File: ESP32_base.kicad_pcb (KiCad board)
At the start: 2 copper layers, 112 x 54.9 mm, 32 parts, among them J1 Conn_01x16_Socket, J2 Conn_01x16_Socket, J3 Conn_01x04_Socket, J5 KH-IPEXA-SMAKWE-B080H, SW1 boot, SW2 reset, U1 ADT7310TRZ, U2 3.3V, U3 ESP32-C5-WROOM-1U-N8-R4

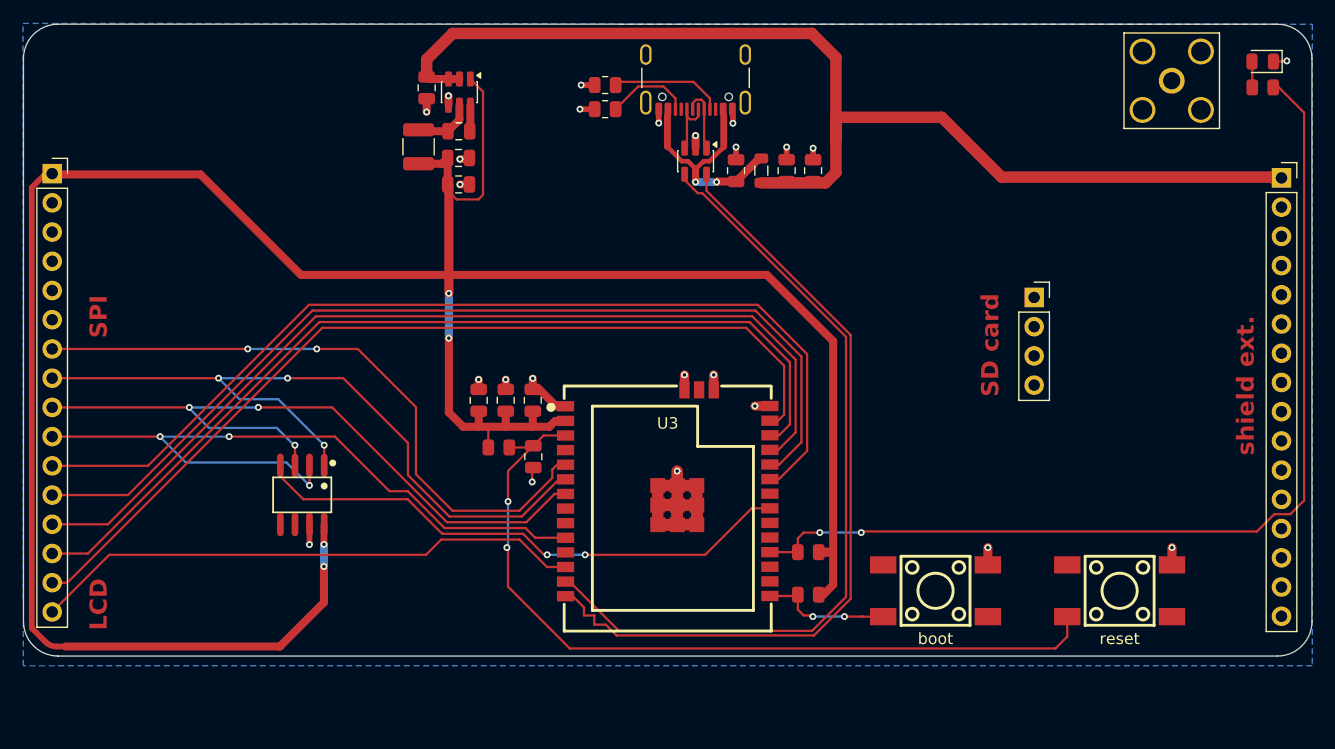
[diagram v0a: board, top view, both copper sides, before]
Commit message: increase signal clearance
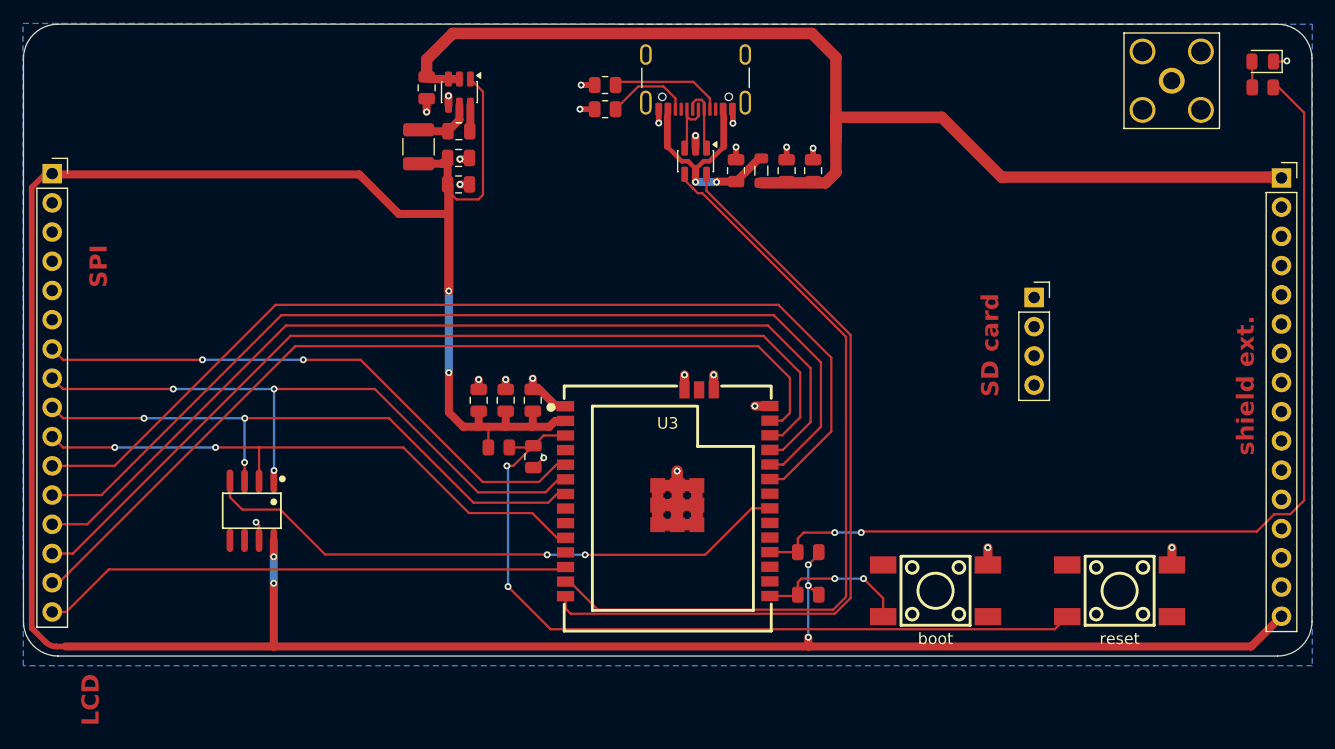
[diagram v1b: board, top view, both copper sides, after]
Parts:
- moved U1 4.59 mm to (103.4, 234.3)
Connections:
- J2 pad 16: unconnected-(J2-Pin_16-Pad16) -> +3.3V
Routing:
- net +3.3V: track 228.7 -> 262.8 mm, vias 4 -> 7
- net /SPI_MISO: track 64.9 -> 51.2 mm, vias 3 -> 2
- net /SPI_SCK: track 65.8 -> 56.6 mm
- net /SPI_MOSI: track 62.4 -> 53.8 mm
- net /JOYSTICK: track 55.9 -> 50.0 mm
- net /TEMP_CS: track 47.4 -> 52.1 mm
- net /TP_IRQ: track 85.5 -> 88.5 mm
- net Net-(U3-EN): track 71.6 -> 69.5 mm
- net /TP_CS: track 84.1 -> 86.1 mm
- net /LCD_DC: track 48.2 -> 46.2 mm
- net Net-(U3-IO28): track 11.5 -> 13.4 mm
- net /USB_D-: track 70.2 -> 68.6 mm
- net /USB_D+: track 70.2 -> 68.6 mm
- net /LCD_BL: track 79.5 -> 78.5 mm
- net /LCD_RST: track 82.5 -> 83.5 mm

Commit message: route EN across MCU
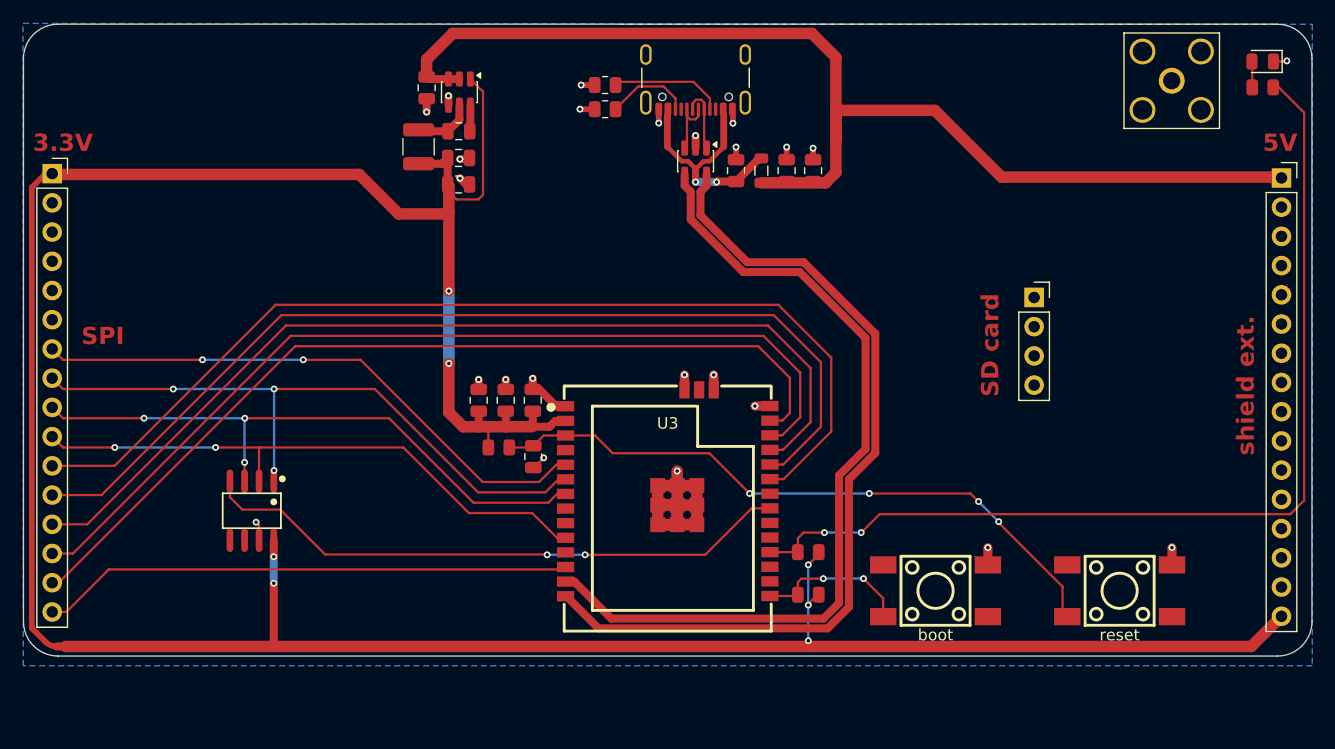
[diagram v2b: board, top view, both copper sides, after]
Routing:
- net Net-(U3-EN): track 69.5 -> 56.8 mm, vias 2 -> 4
- net /USB_D-: track 68.6 -> 74.5 mm
- net /USB_D+: track 68.6 -> 73.3 mm
- net +5V: track 101.9 -> 102.7 mm
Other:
- board text added: "3.3V"
- board text added: "5V"
- board text removed: "LCD"

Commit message: cleanup lower left corner
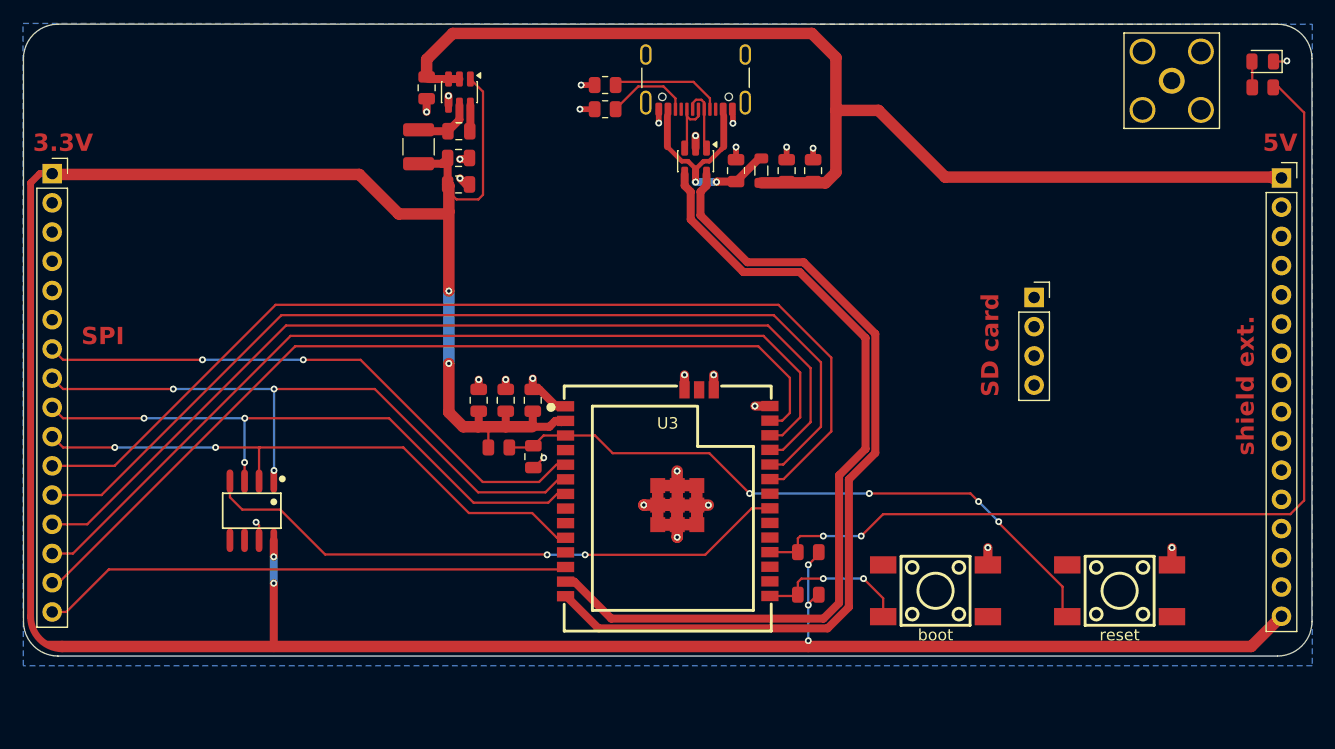
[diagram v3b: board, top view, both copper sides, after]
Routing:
- net +3.3V: track 262.4 -> 258.6 mm
- net GND: track 58.2 -> 61.5 mm, vias 24 -> 27
- net +5V: track 102.7 -> 100.1 mm

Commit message: wip
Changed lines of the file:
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@@
 			)
 		)
-		(property "Datasheet" "~"
+		(property "Datasheet" "https://www.lcsc.com/datasheet/C2905421.pdf"
 			(at 0 0 0)
 			(layer "F.Fab")
@@
 			)
 		)
-		(property "Description" "Generic connector, single row, 01x16, script generated"
+		(property "Description" "Female Header 16 Position 2.54mm Pitch Single Row Through Hole -40℃~+105℃"
 			(at 0 0 0)
 			(layer "F.Fab")
@@
 			)
 		)
+		(property "Part" "KH-2.54FH-1X16P-H8.5"
+			(at 0 0 0)
+			(unlocked yes)
+			(layer "F.Fab")
+			(hide yes)
+			(effects
+				(font
+					(size 1 1)
+					(thickness 0.15)
+				)
+			)
+		)
 		(property ki_fp_filters "Connector*:*_1x??_*")
 		(sheetname "/")
@@
 			)
 		)
-		(property "Datasheet" "~"
+		(property "Datasheet" "https://www.lcsc.com/datasheet/C2905421.pdf"
 			(at 0 0 0)
 			(layer "F.Fab")
@@
 			)
 		)
-		(property "Description" "Generic connector, single row, 01x16, script generated"
+		(property "Description" "Female Header 16 Position 2.54mm Pitch Single Row Through Hole -40℃~+105℃"
 			(at 0 0 0)
 			(layer "F.Fab")
@@
 			)
 		)
+		(property "Part" "KH-2.54FH-1X16P-H8.5"
+			(at 0 0 0)
+			(unlocked yes)
+			(layer "F.Fab")
+			(hide yes)
+			(effects
+				(font
+					(size 1 1)
+					(thickness 0.15)
+				)
+			)
+		)
 		(property ki_fp_filters "Connector*:*_1x??_*")
 		(sheetname "/")
@@
 	)
 	(segment
-		(start 122.3 234.5)
-		(end 127.8 234.5)
+		(start 104.1 228.8)
+		(end 116.6 228.8)
 		(width 0.2)
 		(layer "F.Cu")
@@
 	)
 	(segment
-		(start 104.1 228.8)
-		(end 116.6 228.8)
+		(start 122.3 234.5)
+		(end 127.96 234.5)
 		(width 0.2)
 		(layer "F.Cu")
@@
 	)
 	(segment
-		(start 127.8 234.5)
-		(end 129.95 236.65)
+		(start 91.52 228.8)
+		(end 87.0186 228.8)
 		(width 0.2)
 		(layer "F.Cu")
@@
 	)
 	(segment
-		(start 129.95 236.65)
-		(end 130.7 236.65)
+		(start 127.96 234.5)
+		(end 130.11 236.65)
 		(width 0.2)
 		(layer "F.Cu")
@@
 	)
 	(segment
-		(start 116.6 228.8)
-		(end 122.3 234.5)
+		(start 130.11 236.65)
+		(end 130.7 236.65)
 		(width 0.2)
 		(layer "F.Cu")
@@
 	)
 	(segment
-		(start 91.52 228.8)
-		(end 87.0186 228.8)
+		(start 116.6 228.8)
+		(end 122.3 234.5)
 		(width 0.2)
 		(layer "F.Cu")

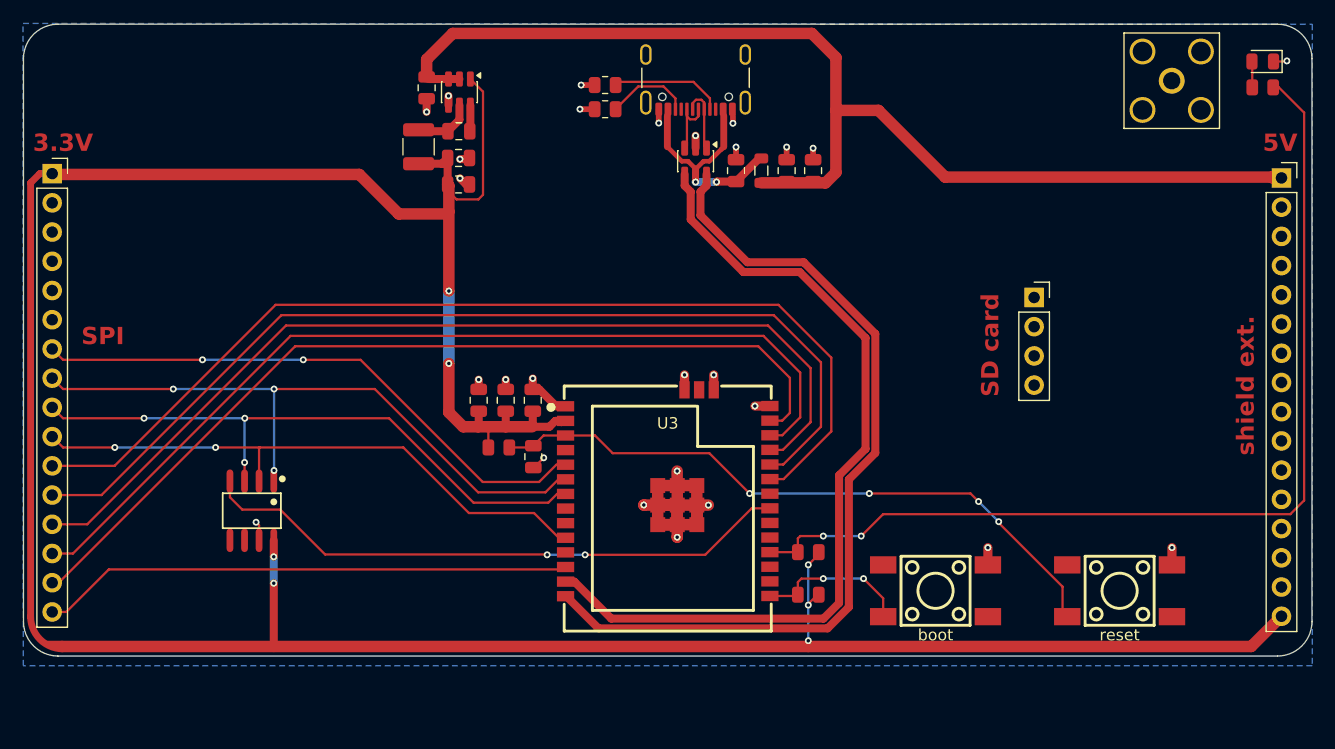
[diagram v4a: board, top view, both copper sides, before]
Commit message: 1206 -> 0805 and no ERC errors
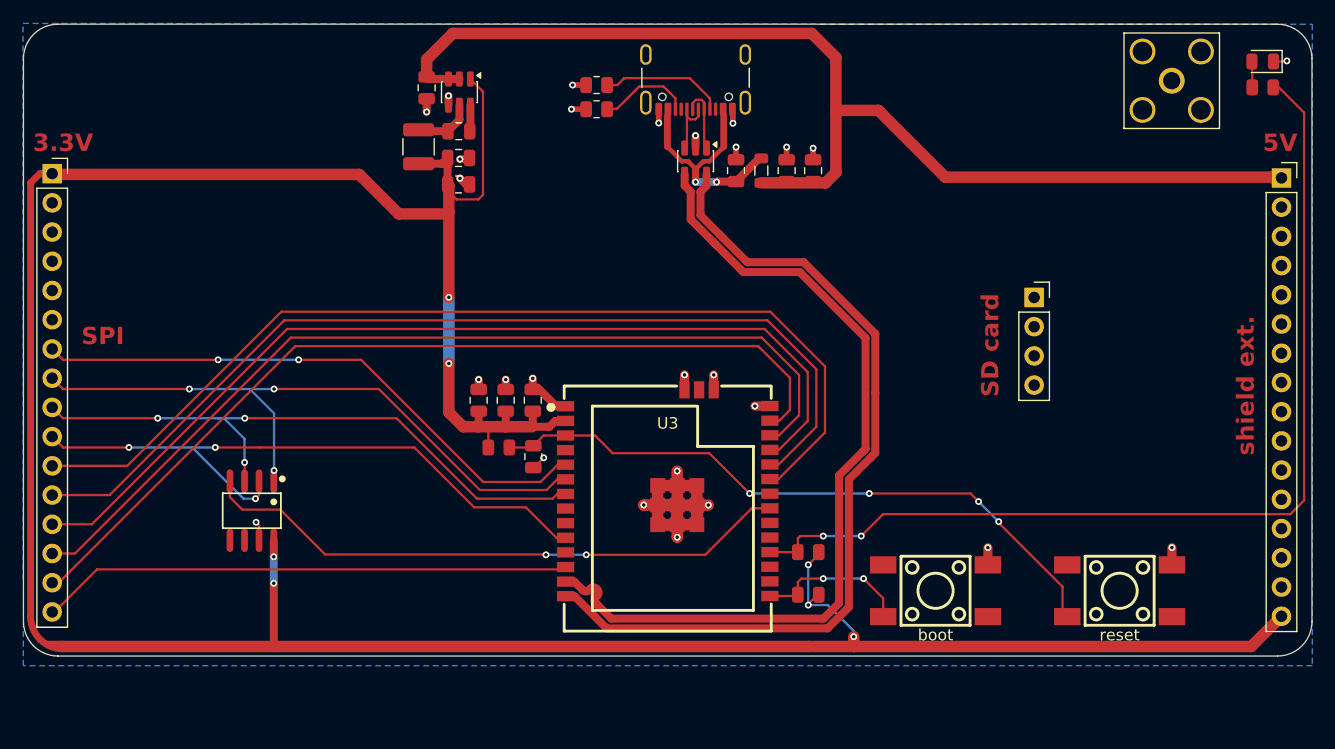
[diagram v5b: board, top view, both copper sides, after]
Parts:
- moved R1 0.74 mm to (133.4, 197.3)
- moved R2 0.74 mm to (133.4, 199.4)
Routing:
- net /SPI_MISO: track 51.2 -> 57.3 mm, vias 2 -> 3
- net +3.3V: track 258.6 -> 260.8 mm
- net /TP_IRQ: track 88.5 -> 86.5 mm
- net /TP_CS: track 86.1 -> 84.6 mm
- net /USB_D+: track 73.3 -> 74.5 mm
- net /LCD_RST: track 83.5 -> 82.5 mm
- net /SPI_MOSI: track 53.8 -> 54.8 mm
- net Net-(USBC1-CC1): track 9.69 -> 10.7 mm
- net /SPI_SCK: track 56.6 -> 57.3 mm
- net /LCD_CS: track 81.0 -> 80.5 mm

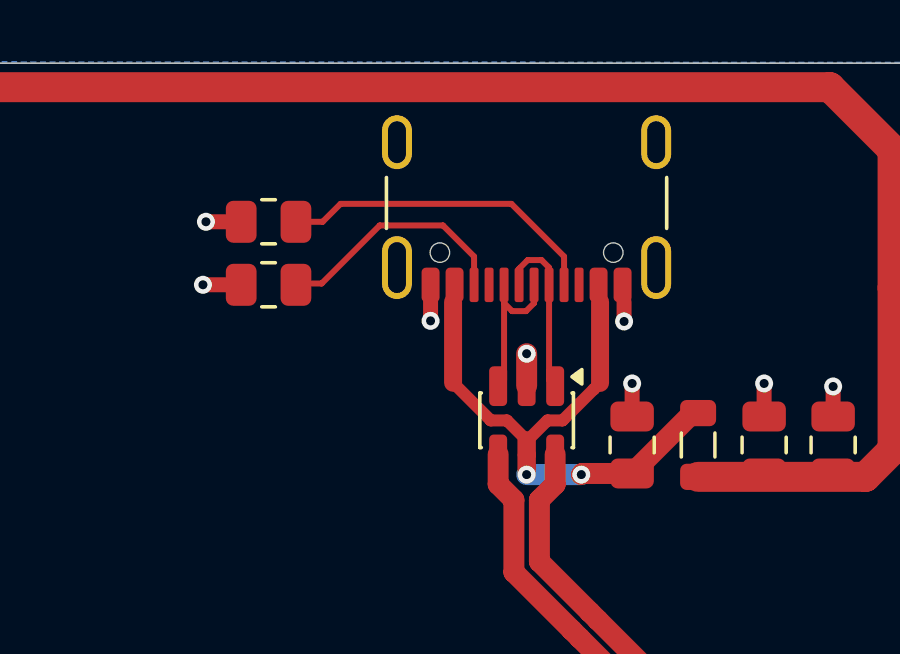
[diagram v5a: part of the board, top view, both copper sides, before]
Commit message: new USBC header
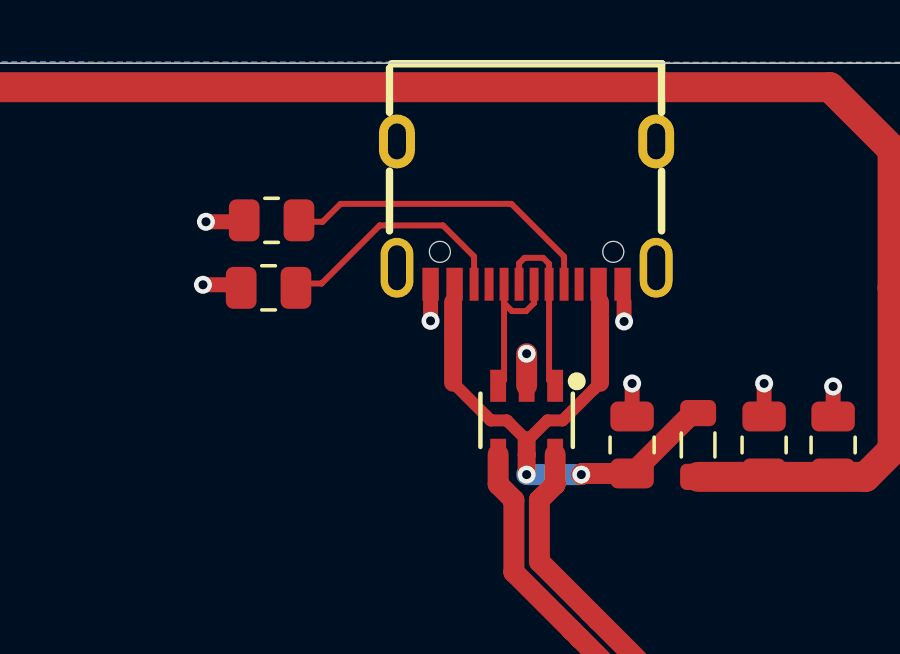
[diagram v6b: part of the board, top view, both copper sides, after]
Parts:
- TVS1: footprint Package_TO_SOT_SMD:SOT-23-6 -> easyeda2kicad:SOT-23-6_L2.9-W1.6-P0.95-LS2.8-BL
- USBC1: value USB_C_Receptacle_USB2.0_16P -> TYPE-C 16PIN 2MD(073); footprint Connector_USB:USB_C_Receptacle_GCT_USB4105-xx-A_16P_TopMnt_Horizontal -> easyeda2kicad:USB-C-SMD_TYPE-C-6PIN-2MD-073
- moved R1 2.20 mm to (133.4, 199.5)
- moved R2 2.15 mm to (133.5, 197.2)
- moved USBC1 1.28 mm to (142.0, 197.0)
- turned TVS1 to 180 degrees
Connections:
- R1 pad 1: Net-(USBC1-CC1) -> Net-(USBC1-CC2)
- R2 pad 1: Net-(USBC1-CC2) -> Net-(USBC1-CC1)
- TVS1 pad 1: Net-(TVS1-Pad1) -> Net-(USBC1-DN1)
- TVS1 pad 3: Net-(TVS1-Pad3) -> Net-(USBC1-DP1)
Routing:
- net Net-(USBC1-DN1): track 0.00 -> 6.04 mm
- net Net-(TVS1-Pad1): track 5.80 -> 0.00 mm
- net Net-(USBC1-DP1): track 0.00 -> 5.69 mm
- net Net-(TVS1-Pad3): track 5.69 -> 0.00 mm

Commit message: wip
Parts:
- TVS1: footprint easyeda2kicad:SOT-23-6_L2.9-W1.6-P0.95-LS2.8-BL -> Package_TO_SOT_SMD:SOT-23-6
- turned TVS1 to -90 degrees

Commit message: remove easyEDA TVS sym
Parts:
- USBC1: footprint easyeda2kicad:USB-C-SMD_TYPE-C-6PIN-2MD-073 -> pwa:USB-C-SMD_TYPE-C-6PIN-2MD-073
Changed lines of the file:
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@@
 		)
 	)
-	(footprint "easyeda2kicad:USB-C-SMD_TYPE-C-6PIN-2MD-073"
+	(footprint "pwa:USB-C-SMD_TYPE-C-6PIN-2MD-073"
 		(layer "F.Cu")
 		(at 142 197 180)
